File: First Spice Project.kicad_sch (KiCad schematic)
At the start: 3 parts

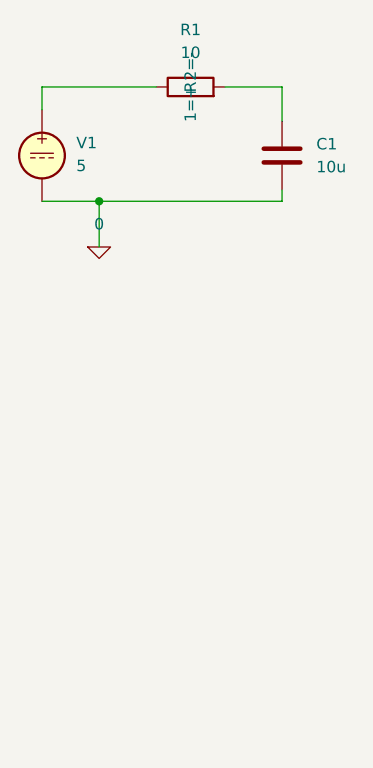
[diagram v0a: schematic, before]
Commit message: added RL and CL circuits and saved sims
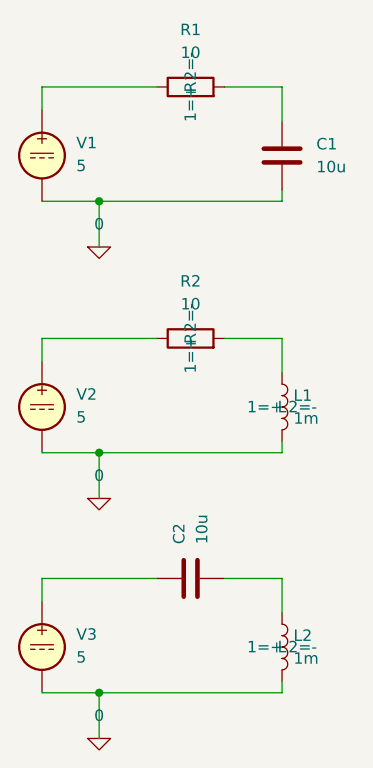
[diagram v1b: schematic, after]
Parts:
- added C2: 10u, symbol Device:C
- added L1, L2: 1m, symbol Device:L
- added R2: 10, symbol Device:R
- added V2, V3: 5, symbol Simulation_SPICE:VDC
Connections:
- net 0: now also L1.2, L2.2, V2.2, V3.2
- new net: L1.1, R2.2
- new net: C2.2, L2.1
- new net: C2.1, V3.1
- new net: R2.1, V2.1
